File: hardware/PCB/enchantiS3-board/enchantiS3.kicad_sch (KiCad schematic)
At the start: 71 parts, among them J1 USB_C_Receptacle_USB2.0, Q1 BSS138, Q2 BSS138, Q3 BSS138, SW1 B3U-1000P, SW2 B3U-1000P, U1 USBLC6-2P6, U2 MCP73871, U3 NCP167AMX330TBG, U4 NCP167AMX180TBG

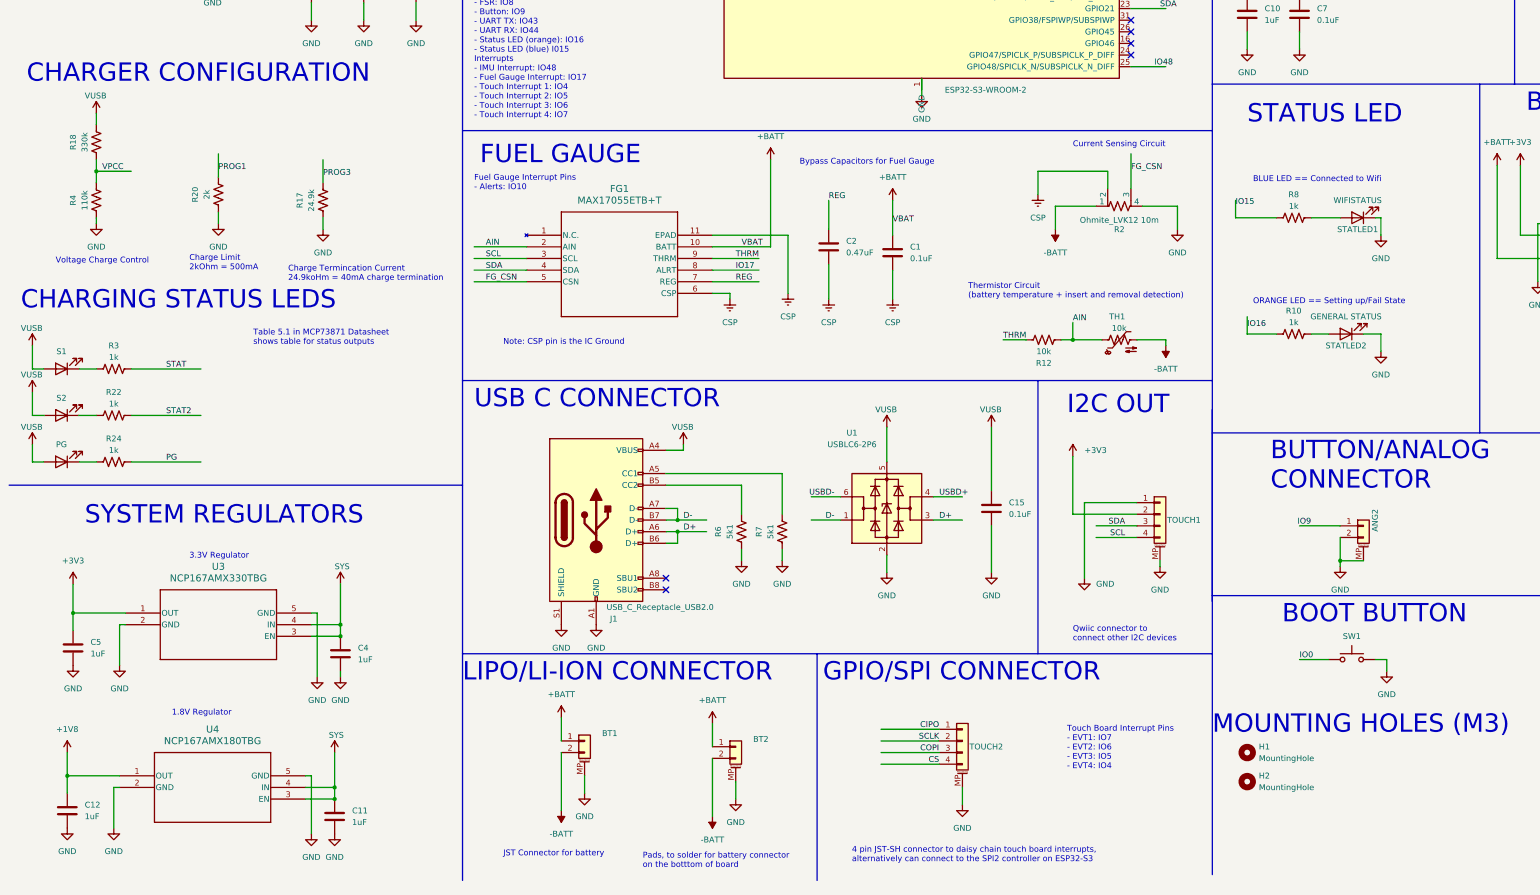
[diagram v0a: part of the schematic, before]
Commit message: updated schematic, added symbol for and gate
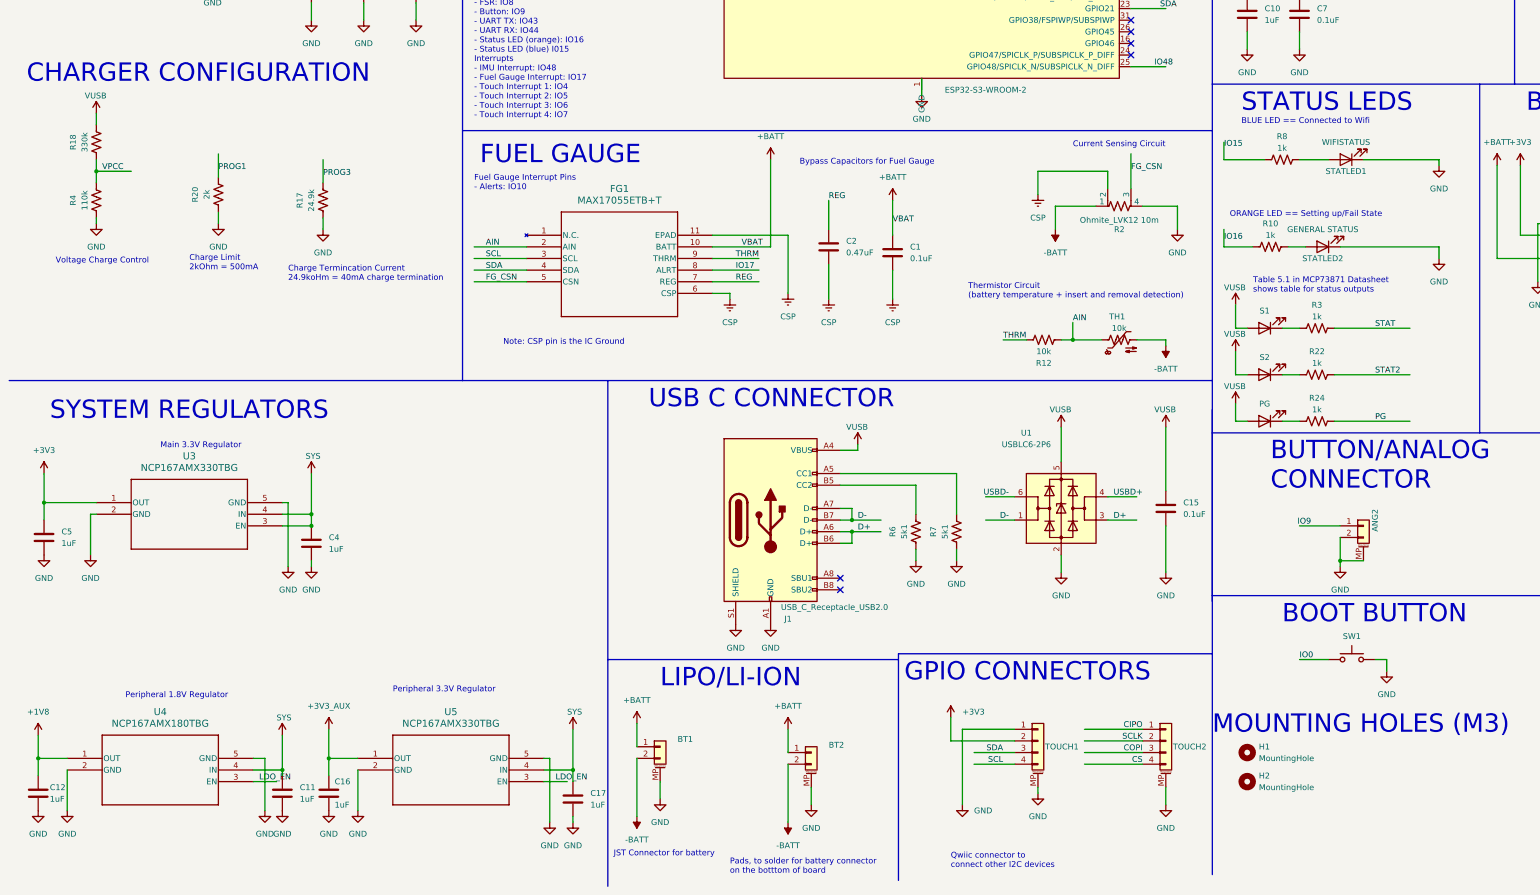
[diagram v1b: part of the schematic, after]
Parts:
- added C16, C17: 1uF, Capacitor_SMD:C_0402_1005Metric, symbol Device:C
- added SYS4: SYS, symbol power-symbols:VSYS
- added U5: NCP167AMX330TBG, XDFN4_1X1_711AJ_ONS, symbol NCP167AMX330TBG:NCP167AMX330TBG
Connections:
- net GND: now also C16.2, C17.2, U5.2 (GND), U5.5 (GND)
- net SYS: now also C17.1, SYS4.1 (SYS), U5.4 (IN); no longer U4.3 (EN)
- new net +3V3_AUX: C16.1, U5.1 (OUT)
- new net LDO_EN: U4.3 (EN), U5.3 (EN)
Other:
- note added: "GPIO CONNECTORS"
- note added: "LIPO/LI-ION"
- note added: "Main 3.3V Regulator"
- note added: "Peripheral 1.8V Regulator"
- note added: "Peripheral 3.3V Regulator"
- note added: "STATUS LEDS"
- note removed: "1.8V Regulator"
- note removed: "3.3V Regulator"
- note removed: "4 pin JST-SH connector to daisy chain touch board interrupts, alternatively can connect to the SPI2 controller on ESP32-S3"
- note removed: "CHARGING STATUS LEDS"
- note removed: "GPIO/SPI CONNECTOR"
- note removed: "I2C OUT"
- note removed: "LIPO/LI-ION CONNECTOR"
- note removed: "STATUS LED"
- note removed: "Touch Board Interrupt Pins - EVT1: IO7 - EVT2: IO6 - EVT3: IO5 - EVT4: IO4"
- moved on the sheet: BT1, BT2, C11, C12, C15, C4, C5, J1, R10, R22, R24, R3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

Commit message: removed, neopixel library, added extra LDO for peripherals
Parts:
- removed Q1, Q2, Q3: BSS138, Package_TO_SOT_SMD:SOT-23, symbol Transistor_FET:BSS138
- removed R21, R23: 2k2, Resistor_SMD:R_0402_1005Metric, symbol Device:R_US
- added C18, C21: 0.1uF, Capacitor_SMD:C_0402_1005Metric, symbol Device:C
- added C20: 1uF, Capacitor_SMD:C_0402_1005Metric, symbol Device:C
- added LDOLED1: LDO2LED, LED_SMD:LED_0402_1005Metric, symbol Device:LED
- added R11: 1k, Resistor_SMD:R_0402_1005Metric, symbol Device:R_US
- added U6: NL17SV08XV5T2G, SOT553-5_ONS, symbol NL17SV08:NL17SV08XV5T2G
- added U7: max3378eetd+t, 21-0137I_T1433-2_MXM, symbol MAX3378E:max3378eetd+t
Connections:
- net +1V8: now also C18.1, U7.10 (VL), U7.3 (*THREE-STATE)
- net +3V3: now also C20.1, C21.1, U6.1, U6.5 (VCC), U7.14 (VCC); no longer TOUCH1.2 (Pin_2)
- net +3V3_AUX: now also TOUCH1.2 (Pin_2)
- net GND: now also C18.2, C20.2, C21.2, LDOLED1.1 (K), U6.3 (GND), U7.15 (EPAD), U7.7 (GND)
- net IMU_INT: now also U7.2 (I/O_VL2)
- net IO39: now also U6.2
- net IO48: now also U7.12 (I/O_VCC2)
- net LDO_EN: now also R11.1, U6.4; no longer U4.3 (EN)
- net LV_SCL: now also U7.1 (I/O_VL1)
- net LV_SDA: now also U7.5 (I/O_VL3)
- net SCL: now also U7.13 (I/O_VCC1)
- net SDA: now also U7.9 (I/O_VCC3)
- net SYS: now also U4.3 (EN)
- new net: LDOLED1.2 (A), R11.2
- no-connect marks 9 -> 11
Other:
- note added: "1.8V Regulator"
- note added: "LED indicator for LDO2"
- note removed: "D"
- note removed: "G"
- note removed: "Peripheral 1.8V Regulator"
- note removed: "S"
- moved on the sheet: C10, C11, C12, C16, C17, C6, C7, IMU1, R14, R15, R16, U4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

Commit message: updated schematic
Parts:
- removed LDOLED1: LDO2LED, LED_SMD:LED_0402_1005Metric, symbol Device:LED
- removed R11: 1k, Resistor_SMD:R_0402_1005Metric, symbol Device:R_US
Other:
- note added: "CHARGER CONFIG"
- note added: "Charge Termination Current 24.9koHm = 40mA charge termination"
- note removed: "CHARGER CONFIGURATION"
- note removed: "Charge Limit 2kOhm = 500mA"
- note removed: "Charge Termincation Current 24.9koHm = 40mA charge termination"
- note removed: "LED indicator for LDO2"
- moved on the sheet: R17, R18, R20, R4

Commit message: updated text in schematic
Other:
- note added: "Charge resistor 1k = 1000mA 2k = 500mA 5k = 100mA"
- moved on the sheet: R17, R18, R20, R4, U6

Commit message: upadated schematic, connected IMU data pins to SPI line, updated manufacturing files
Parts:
- removed R14, R15: 2k2, Resistor_SMD:R_0402_1005Metric, symbol Device:R_US
- removed U6: NL17SV08XV5T2G, SOT553-5_ONS, symbol NL17SV08:NL17SV08XV5T2G
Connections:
- net IO39 is gone; now on net COPI_AUX: MCU1.32 (MTCK/GPIO39/CLK_OUT3/SUBSPICS1)
- net +1V8: no longer IMU1.22 (~{CS})
- net GND: no longer IMU1.9 (SDO/AD0)
- net LDO_EN: now also MCU1.25 (GPIO48/SPICLK_N/SUBSPICLK_N_DIFF)
- net SCL: no longer U7.13 (I/O_VCC1)
- net SDA: no longer U7.9 (I/O_VCC3)
- net COPI_1V8: now reaches U7.6 (I/O_VL4)
- net COPI_1V8: now also IMU1.24 (SDA/SDI)
- net COPI_AUX: now reaches U7.8 (I/O_VCC4)
- net IMU_INT: no longer names the net of IMU1.12 (INT1)
- net IMU_INT: no longer U7.2 (I/O_VL2)
- net IO40 renamed CIPO_AUX
- net CIPO_AUX: now also U7.9 (I/O_VCC3)
- net IO41 renamed CS_AUX
- net CS_AUX: now also U7.12 (I/O_VCC2)
- net IO42 renamed CLK_AUX
- net CLK_AUX: now also U7.13 (I/O_VCC1)
- removed net IO48: MCU1.25 (GPIO48/SPICLK_N/SUBSPICLK_N_DIFF), U7.12 (I/O_VCC2)
- net LV_SCL renamed CLK_1V8
- net LV_SDA renamed CIPO_1V8
- net CIPO_1V8: now also IMU1.9 (SDO/AD0); no longer IMU1.24 (SDA/SDI)
- new net CS_1V8: IMU1.22 (~{CS}), U7.2 (I/O_VL2)
- no-connect marks 11 -> 10
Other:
- note removed: "I2C Level Shifting"
- moved on the sheet: C18, C20, C21

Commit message: updated BOM and manufacturing files
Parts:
- R22: value 1k -> 2k; Description Value Pkg 1 kOhms ±1% 0.1W, 1/10W Chip Resistor 0402 (1005 Metric) Au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 -> 2 kOhms ±1% 0.1W, 1/10W Chip Resistor 0402 (1005 Metric) Au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
- R24: value 1k -> 470; Description Value Pkg 1 kOhms ±1% 0.1W, 1/10W Chip Resistor 0402 (1005 Metric) Au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 -> 470 Ohms ±1% 0.1W, 1/10W Chip Resistor 0402 (1005 Metric) A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; Mfg Part # ERJ-2RKF1001X -> ERJ-2RKF4700X
- R3: value 1k -> 2k; Description Value Pkg 1 kOhms ±1% 0.1W, 1/10W Chip Resistor 0402 (1005 Metric) Au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 -> 2 kOhms ±1% 0.1W, 1/10W Chip Resistor 0402 (1005 Metric) Au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; Mfg Part # ERJ-2RKF1001X -> ERJ-2RKF2001X
- U7: Description Value Pkg (none) -> Voltage Level Translator Bidirectional 1 Circuit 4 Channel 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; Manufacturer (none) -> Analog Devices Inc./Maxim Integrated; Mfg Part # (none) -> MAX3378EETD+T
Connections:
- net LDO_EN: now also U4.3 (EN)
- net SYS: no longer U4.3 (EN)
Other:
- note added: "Comms - USBD+: IO20 - USBD-: IO19 - UART TX: IO43 - UART RX: IO44 I2C - SDA: IO21 - SCL: IO14 SPI - COPI: 10 - CIPO: 13 - SCLK: 12 - CS0: 11 - COPI_AUX: 39 - CIPO_AUX: 40 - CLK_AUX: 42 - CS_AUX: 41 Peripherals - LDO ENABLE: 48 - FSR: IO8 - Button: IO9 - Status LED (orange): IO16 - Status LED (blue) I015 Interrupts - Fuel Gauge Interrupt: IO17"
- note added: "ESD Protection IC"
- note removed: "Comms - SDA: IO21 - SCL: IO14 - USBD+: IO20 - USBD-: IO19 - COPI: 10 - CIPO: 13 - SCLK: 12 - CS0: 11 Peripherals - FSR: IO8 - Button: IO9 - UART TX: IO43 - UART RX: IO44 - Status LED (orange): IO16 - Status LED (blue) I015 Interrupts - IMU Interrupt: IO48 - Fuel Gauge Interrupt: IO17 - Touch Interrupt 1: IO4 - Touch Interrupt 2: IO5 - Touch Interrupt 3: IO6 - Touch Interrupt 4: IO7"
- moved on the sheet: BT1, BT2, C10, C11, C12, C13, C15, C16, C17, C18, C19, C20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
